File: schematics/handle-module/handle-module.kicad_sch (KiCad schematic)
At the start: 34 parts, among them J1 Conn_01x02_Socket, J11 USBASP, J2 XY-MK-5V@433MHz, J3 FS1000A@433Mhz, Q10 IRLML5203, Q14 IRLML0030, SW1 Close, SW2 Open, U1 AMS1117-5.0, U13 ATtiny1616-M, X2 CSX-750FCC, 16MHz

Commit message: Creating schematics and boards
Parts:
- removed C19 (x4): 22 uF, Capacitor_SMD:C_1210_3225Metric, symbol Device:C
- removed C22, C29: 100 nF, Capacitor_SMD:C_0603_1608Metric, symbol Device:C
- removed J11: USBASP, Connector_PinHeader_2.54mm:PinHeader_2x05_P2.54mm_Vertical, symbol Connector_Generic:Conn_02x05_Odd_Even
- removed J2: XY-MK-5V@433MHz, symbol Connector:Conn_01x04_Socket
- removed JP4: Jumper_2_Open, TestPoint:TestPoint_2Pads_Pitch2.54mm_Drill0.8mm, symbol Jumper:Jumper_2_Open
- removed Q14: IRLML0030, Package_TO_SOT_SMD:SOT-23, symbol Transistor_FET:IRLML0030
- removed R15, R29: 10K, Resistor_SMD:R_0805_2012Metric, symbol Device:R
- removed R15 (x2): 8K2, Resistor_SMD:R_0805_2012Metric, symbol Device:R
- removed U1: AMS1117-5.0, Package_TO_SOT_SMD:SOT-223-3_TabPin2, symbol Regulator_Linear:AMS1117-3.3
- removed U13: ATtiny1616-M, Package_DFN_QFN:VQFN-20-1EP_3x3mm_P0.4mm_EP1.7x1.7mm, symbol MCU_Microchip_ATtiny:ATtiny1616-M
- removed X2: CSX-750FCC, 16MHz, Oscillator:Oscillator_SMD_Abracon_ASE-4Pin_3.2x2.5mm, symbol Oscillator:SG-211
- added C14, C18, C21, C26 (x8): 100 nF, Capacitor_SMD:C_0603_1608Metric, symbol Device:C
- added C18, C26 (x2): 1 uF, Capacitor_SMD:C_0603_1608Metric, symbol Device:C
- added C26 (x2): 47 nF, Capacitor_SMD:C_0603_1608Metric, symbol Device:C
- added C26 (x4): 2.2 uF, Capacitor_SMD:C_0603_1608Metric, symbol Device:C
- added C26: 10 nF, Capacitor_SMD:C_0603_1608Metric, symbol Device:C
- added C26: 10 uF, Capacitor_SMD:C_0603_1608Metric, symbol Device:C
- added C26: 1 nF, Capacitor_SMD:C_0603_1608Metric, symbol Device:C
- added C27, C28: 15 pF, Capacitor_SMD:C_0603_1608Metric, symbol Device:C
- added C29 (x7): 22 uF, Capacitor_SMD:C_1210_3225Metric, symbol Device:C
- added C5, C6: 100 uF, Capacitor_THT:CP_Radial_D6.3mm_P2.50mm, symbol Device:C_Polarized
- added D10, D9: ES2J, Diode_SMD:D_SMB, symbol Device:D
- added D16: BAV21WS, Diode_SMD:D_SOD-323F, symbol Device:D
- added D2, D7, D8: 15MQ030NPBF, Diode_SMD:D_SMA, symbol Device:D
- added F1, F2: 3A, Library:FuseHolder1808, symbol Device:Fuse
- added H1, H2, H3, H4: MountingHole, MountingHole:MountingHole_2.2mm_M2, symbol Mechanical:MountingHole
- added J2: JST XH B3B, symbol Connector:Conn_01x03_Pin
- added J4: USBASP, Connector_PinHeader_2.54mm:PinHeader_2x05_P2.54mm_Vertical, symbol Connector_Generic:Conn_02x05_Odd_Even
- added JP1: AC Detect, Jumper:SolderJumper-2_P1.3mm_Open_TrianglePad1.0x1.5mm, symbol Jumper:SolderJumper_2_Open
- added L1, L2: ?, symbol Device:L
- added L3: AMPLF0630, 8,2uH, Inductor_SMD:L_Abracon_ASPI-0630LR, symbol Device:L
- added NT1: AGND/PGND, NetTie:NetTie-2_SMD_Pad2.0mm, symbol Device:NetTie_2
- added Q3 (x8): IRLML0030, Package_TO_SOT_SMD:SOT-23, symbol Transistor_FET:IRLML0030
- added R15 (x4): 100K, Resistor_SMD:R_0805_2012Metric, symbol Device:R
- added R15 (x4): 10, Resistor_SMD:R_0805_2012Metric, symbol Device:R
- added R15: 2R, Resistor_SMD:R_0805_2012Metric, symbol Device:R
- added R15 (x5), R28 (x3): 10K, Resistor_SMD:R_0805_2012Metric, symbol Device:R
- added R15: 45K, Resistor_SMD:R_0805_2012Metric, symbol Device:R
- added R15: 4R7, Resistor_SMD:R_0805_2012Metric, symbol Device:R
- added R15 (x2): 0.01 R, Resistor_SMD:R_1206_3216Metric, symbol Device:R
- added R15: 6R8, Resistor_SMD:R_0805_2012Metric, symbol Device:R
- added R15 (x3): 4K, Resistor_SMD:R_0805_2012Metric, symbol Device:R
- added R15: 7K, Resistor_SMD:R_0805_2012Metric, symbol Device:R
- added RV1: JVR-05N180M, Varistor:RV_Disc_D7mm_W4.5mm_P5mm, symbol Device:Varistor
- added TP1: VBAT, TestPoint:TestPoint_Pad_D1.0mm, symbol Connector:TestPoint
- added TP2: GND, TestPoint:TestPoint_Plated_Hole_D2.0mm, symbol Connector:TestPoint
- added TP3: +5V, TestPoint:TestPoint_Pad_D1.0mm, symbol Connector:TestPoint
- added TP4: VSYS, TestPoint:TestPoint_Pad_D1.0mm, symbol Connector:TestPoint
- added TP5: CHG SUPPLY, TestPoint:TestPoint_Pad_D1.0mm, symbol Connector:TestPoint
- added TP6: ILIM, TestPoint:TestPoint_Pad_D1.0mm, symbol Connector:TestPoint
- added U1: STX882@443MHz, Library:STX882_Vertical, symbol My_Library:STX882
- added U12: ATmega328-A, Package_QFP:TQFP-32_7x7mm_P0.8mm, symbol MCU_Microchip_ATmega:ATmega328-A
- added U2: SRX882@443MHz, Library:SRX882_Vertical, symbol My_Library:SRX882
- added U3: AMS1117-5.0, Package_TO_SOT_SMD:SOT-223-3_TabPin2, symbol Regulator_Linear:AMS1117-5.0
- added U4: MCP1703T-3302E, Package_TO_SOT_SMD:SOT-23, symbol Regulator_Linear:AMS1117-3.3
- added U6: BQ24780S, Package_DFN_QFN:QFN-28-1EP_4x4mm_P0.4mm_EP2.6x2.6mm_ThermalVias, symbol My_Library:BQ24780S
- added X1: HC-49U, 8MHz, Crystal:Crystal_HC49-U_Vertical, symbol Device:Crystal
- J1: value Conn_01x02_Socket -> 2*LiFePo4@18650@1800mAh, 6,4V; footprint (none) -> Connector_PinSocket_2.54mm:PinSocket_1x02_P2.54mm_Vertical
- J3: value FS1000A@433Mhz -> JST XH B3B; footprint (none) -> Connector_JST:JST_XH_B3B-XH-A_1x03_P2.50mm_Vertical
- SW1: renamed from SW2; value Open -> KLS7-TS3601-5.0-180; footprint (none) -> Library:SW_PUSH_P6.5_W3.5; Поле4 (none) -> Open
- SW2: renamed from SW1; value Close -> KLS7-TS3601-5.0-180; footprint (none) -> Library:SW_PUSH_P6.5_W3.5; Поле4 (none) -> Close
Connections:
- net POWER_UP_SW2 is gone; now on net OPEN_BUTTON: D16.2 (A), SW1.2
- net +5V: now also C14.1, C21.1, C26.1, C26.1, C29.1, J4.2 (Pin_2), R15.2, R15.2, R15.2, R15.2, R28.1, R28.1, R28.2, TP3.1, U1.3 (VCC), U12.18 (AVCC), U12.20 (AREF), U12.4 (VCC), U12.6 (VCC), U2.3 (VCC), U2.4 (CS), U3.2 (VO); no longer J3.2 (Pin_2)
- net CLOSE_BUTTON: now also D16.2 (A), SW2.1, Q3.1 (G)
- net FM_IN: now also U12.11 (PD7), U2.5 (DATA)
- net FM_OUT: now also U1.2 (DATA), U12.1 (PD3); no longer J3.1 (Pin_1)
- net LED_GREEN#: now also U12.13 (PB1)
- net LED_RED#: now also U12.14 (PB2)
- net OPEN_BUTTON: now also Q3.1 (G)
- net POWER_UP_IC: now also U12.9 (PD5)
- net GNDPWR: now reaches J1.1 (Pin_1)
- net GNDPWR: now also J3.2 (Pin_2), C26.2, C26.2, C26.2, C29.2, C29.2, C29.2, C5.2, NT1.1, Q3.2 (S), R15.2, RV1.2, TP2.1, U6.29 (PGND)
- removed net +9V: J1.2 (Pin_2), SW1.1, SW2.1
- net GND renamed GNDA
- net GNDA: now also C14.2, C18.1, C18.1, C21.2, C26.1, C26.2, C26.2, C26.2, C26.2, C26.2, C26.2, C26.2, C26.2, C27.2, C28.2, C29.2, C29.2, C29.2, C29.2, C6.2, J4.10 (Pin_10), J4.8 (Pin_8), NT1.2, Q3.2 (S), Q3.2 (S), Q3.2 (S), R15.1, R15.2, R15.2, R15.2, U1.4 (GND), U12.21 (GND), U12.3 (GND), U12.5 (GND), U2.2 (GND), U2.6 (GND), U3.1 (GND), U4.1 (GND), U6.22 (AGND); no longer J3.3 (Pin_3)
- net POWER_UP: no longer names the net of D16.1 (K), D16.1 (K), D16.1 (K)
- net POWER_UP: now also D16.1 (K), Q3.1 (G), R15.1
- net POWER_UP_SW1 renamed VBAT
- net VBAT: now also SW1.1, C26.1, C26.2, C29.1, D8.2 (A), F1.2, R15.1, R15.2, R15.2, TP1.1; no longer D16.2 (A)
- new net: C26.1, R15.1, U6.28 (VCC)
- new net: C26.2, C26.2, Q3.1 (G), R15.1, R15.2
- new net: C26.2, Q3.3 (D), R15.1, R15.2, U6.13 (CMPIN)
- new net: C26.1, D9.2 (A), J3.3 (Pin_3)
- new net: C26.2, D10.2 (A), J3.1 (Pin_1)
- new net: C26.2, R15.1
- new net: C28.1, U12.8 (XTAL2/PB7), X1.1
- new net: C27.1, U12.7 (XTAL1/PB6), X1.2
- new net: D7.1 (K), D8.1 (K), R15.2
- new net: R15.1, U6.5 (ACOK)
- new net: D10.1 (K), D9.1 (K), F2.1
- new net: C26.1, C26.1, Q3.3 (D), R15.1, U6.2 (ACP)
- new net: C29.1, D2.1 (K), U3.3 (VI)
- new net: JP1.1 (A), R15.1, R15.2
- new net: JP1.2 (B), U6.6 (ACDET)
- new net: J2.1 (Pin_1), L2.1
- new net: J2.2 (Pin_2), L1.1, L2.2
- new net: Q3.1 (G), R15.1
- new net: C26.1, R15.1
- new net: R15.1, U6.16 (TB_STAT#)
- new net: R15.2, U6.17 (BATSRC)
- new net: R15.2, U6.18 (BATDRV)
- new net: Q3.1 (G), U6.23 (LODRV)
- new net: C26.1, U6.24 (REGN)
- new net: Q3.1 (G), U6.26 (HIDRV)
- new net: R15.2, U6.3 (CMSRC)
- new net: R15.2, U6.4 (ACDRV)
- new net: J2.3 (Pin_3), L1.2
- new net +3V3: C18.2, R15.1, U4.2 (VO)
- new net CHARGER_BATDRV: Q3.1 (G), R15.1
- new net CHARGER_BATSRC: C26.1, C26.1, L3.2, Q3.2 (S), R15.1, R15.1, R15.2
- new net CHARGER_BOOST: R15.2, U6.25 (BTST)
- new net CHARGER_ILIM: R15.1, R15.2, TP6.1, U6.21 (ILIM)
- new net CHARGER_PHASE: C26.2, L3.1, Q3.2 (S), Q3.3 (D), U6.27 (PHASE)
- new net CHARGER_SRN: R15.2, U6.19 (SRN)
- new net CHARGER_SRP: R15.1, U6.20 (SRP)
- new net CHARGER_SUPPLY: C26.1, C26.1, C26.1, D16.2 (A), D7.2 (A), F2.2, Q3.3 (D), R15.1, RV1.1, TP5.1
- new net CHR_VSYS_NMOS: C26.1, Q3.2 (S), Q3.2 (S), R15.1
- new net CLOSE_BUTTON_5V#: Q3.3 (D), R15.1, U12.12 (PB0)
- new net MISO: J4.9 (Pin_9), U12.16 (PB4)
- new net MOSI: J4.1 (Pin_1), U12.15 (PB3)
- new net OPEN_BUTTON_5V#: Q3.3 (D), R15.1, U12.10 (PD6)
- new net RESET#: C26.1, J4.5 (Pin_5), R28.1, U12.29 (~{RESET}/PC6)
- new net RXD: J4.4 (Pin_4), U12.30 (PD0)
- new net SCK: J4.7 (Pin_7), U12.17 (PB5)
- new net SCL: R28.2, U12.28 (PC5), U6.12 (SCL)
- new net SDA: R28.2, U12.27 (PC4), U6.11 (SDA)
- new net TXD: J4.6 (Pin_6), U12.31 (PD1)
- new net VBAT_BEFORE_FUSE: C18.2, C26.1, C29.1, C5.1, C6.1, F1.1, J1.2 (Pin_2)
- new net VSYS: C26.1, C26.2, C29.1, C29.1, C29.1, D2.2 (A), Q3.3 (D), Q3.3 (D), R15.2, TP4.1, U4.3 (VI), U6.1 (ACN)
- no-connect marks 7 -> 16
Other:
- note added: "0.1A"
- note added: "0.5A"
- note added: "2A"
- note added: "AVG 1A MAX 2A"
- note added: "Program ATMega"
- note added: "REG0x3B[7] = 1"
- note added: "Test required"
- note removed: "ATTiny program port"
- note removed: "vdd cap"
- moved on the sheet: C18, D16, D8, J1, Q10, R15, R18, R54, SW1, SW2

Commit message: Second board
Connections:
- net GNDA: now also C26.2
- net GNDPWR: no longer C26.2
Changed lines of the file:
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@@
     )
   )
+  (symbol (lib_id "power:GNDA") (at 358.14 140.97 0) (unit 1)
+    (in_bom yes) (on_board yes) (dnp no)
+    (property "Reference" "#PWR053" (at 358.14 147.32 0)
+      (effects (font (size 1.27 1.27)) hide)
+    )
+    (property "Value" "GNDA" (at 358.14 146.05 0)
+      (effects (font (size 1.27 1.27)))
+    )
+    (property "Footprint" "" (at 358.14 140.97 0)
+      (effects (font (size 1.27 1.27)) hide)
+    )
+    (property "Datasheet" "" (at 358.14 140.97 0)
+      (effects (font (size 1.27 1.27)) hide)
+    )
+    (pin "1")
+    (instances
+      (project "handle-module"
+        (path "/5a1662b2-39be-45fc-af40-ee8b9104876f"
+          (reference "#PWR053") (unit 1)
+        )
+      )
+    )
+  )
   (symbol (lib_id "Device:C") (at 323.85 351.79 0) (unit 1)
     (in_bom yes) (on_board yes) (dnp no) (fields_autoplaced)
@@
         )
       )
-    )
-  )
-  (symbol (lib_id "power:GNDPWR") (at 358.14 140.97 0) (unit 1)
-    (in_bom yes) (on_board yes) (dnp no)
-    (property "Reference" "#PWR053" (at 358.14 146.05 0)
-      (effects (font (size 1.27 1.27)) hide)
-    )
-    (property "Value" "GNDPWR" (at 358.013 144.78 0)
-      (effects (font (size 1.27 1.27)))
-    )
-    (property "Footprint" "" (at 358.14 142.24 0)
-      (effects (font (size 1.27 1.27)) hide)
-    )
-    (property "Datasheet" "" (at 358.14 142.24 0)
-      (effects (font (size 1.27 1.27)) hide)
-    )
-    (pin "1")
-    (instances
-      (project "handle-module"
-        (path "/5a1662b2-39be-45fc-af40-ee8b9104876f"
-          (reference "#PWR053") (unit 1)
-        )
-      )

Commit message: Project prepared to order
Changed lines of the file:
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@@
     (stroke (width 0) (type default))
   )
+  (wire (pts (xy 153.67 21.59) (xy 153.67 26.67))
+    (stroke (width 0) (type default))
+  )
   (wire (pts (xy 215.9 124.46) (xy 233.68 124.46))
     (stroke (width 0) (type default))
@@
     (effects (font (size 1.27 1.27)) (justify right bottom))
   )
+  (label "VSYS" (at 153.67 26.67 270) (fields_autoplaced)
+    (effects (font (size 1.27 1.27)) (justify right bottom))
+  )
   (label "CHARGER_BATSRC" (at 421.64 154.94 180) (fields_autoplaced)
     (effects (font (size 1.27 1.27)) (justify right bottom))
@@
         )
       )
+    )
+  )
+  (symbol (lib_id "power:PWR_FLAG") (at 153.67 21.59 0) (unit 1)
+    (in_bom yes) (on_board yes) (dnp no) (fields_autoplaced)
+    (property "Reference" "#FLG07" (at 153.67 19.685 0)
+      (effects (font (size 1.27 1.27)) hide)
+    )
+    (property "Value" "PWR_FLAG" (at 153.67 16.51 0)
+      (effects (font (size 1.27 1.27)))
+    )
+    (property "Footprint" "" (at 153.67 21.59 0)
+      (effects (font (size 1.27 1.27)) hide)
+    )
+    (property "Datasheet" "~" (at 153.67 21.59 0)
+      (effects (font (size 1.27 1.27)) hide)
+    )
+    (pin "1")
+    (instances
+      (project "handle-module"
+        (path "/5a1662b2-39be-45fc-af40-ee8b9104876f"
+          (reference "#FLG07") (unit 1)
+        )
+      )

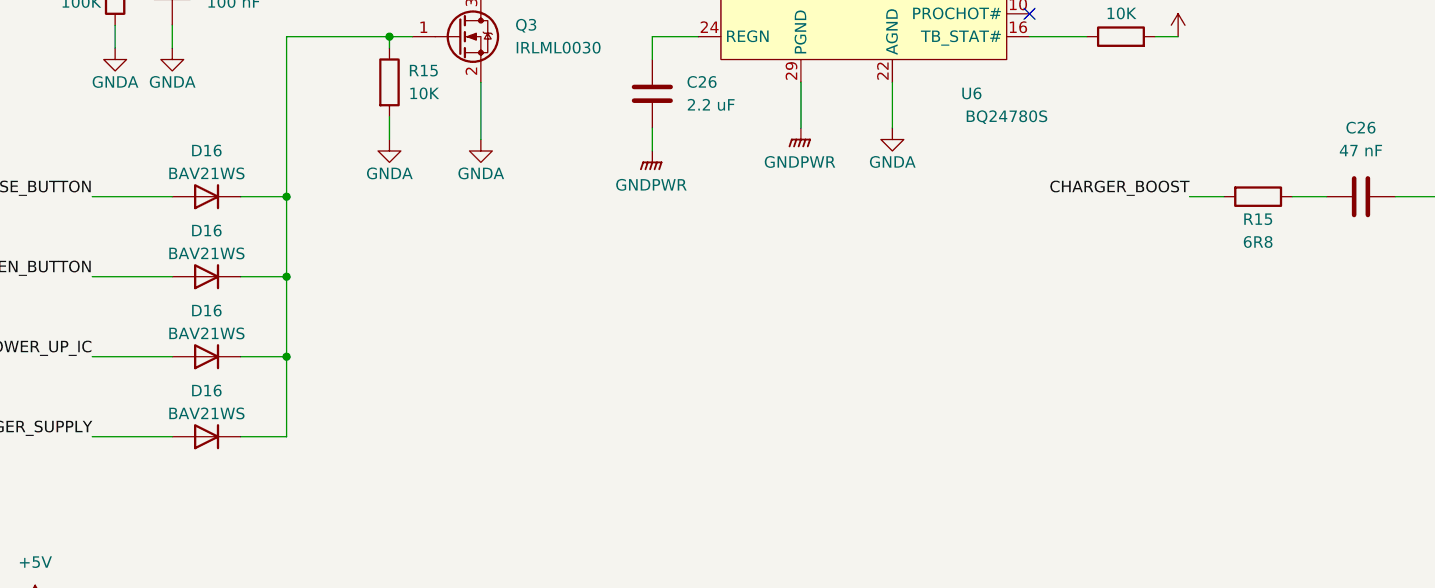
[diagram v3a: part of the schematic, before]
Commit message: first version of main-module firmware. not tested yet.
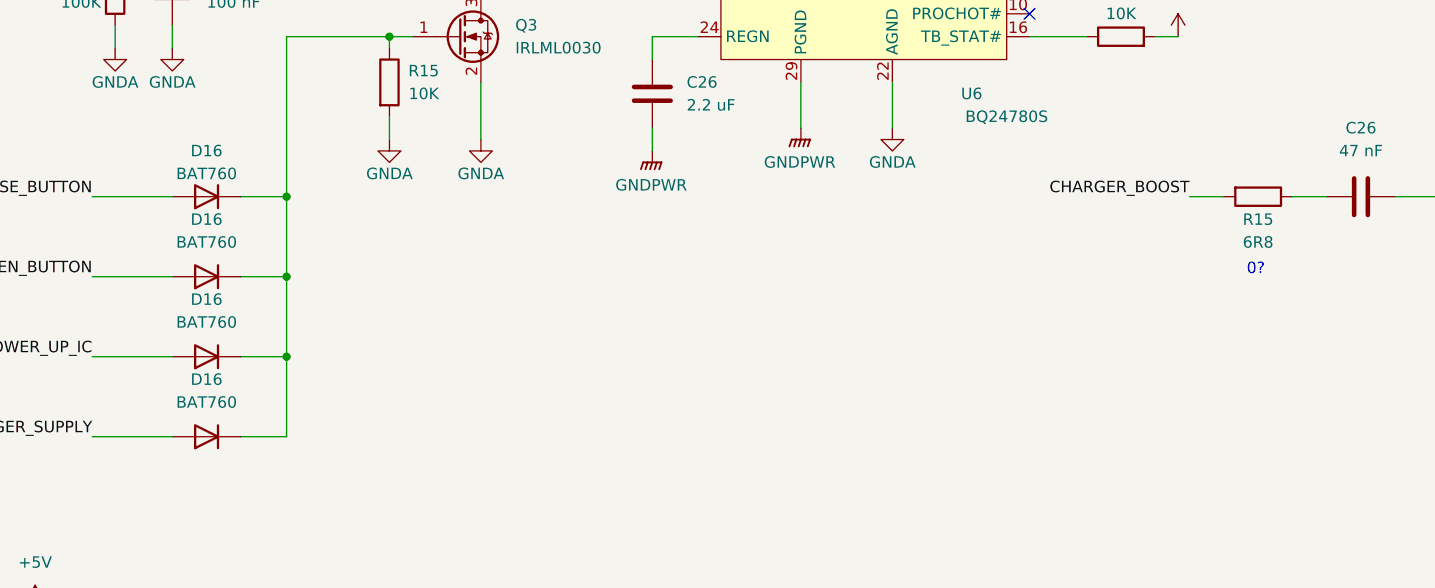
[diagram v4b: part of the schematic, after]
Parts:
- D16: value BAV21WS -> BAT760
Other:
- note added: "0?"
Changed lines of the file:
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@@
     (effects (font (size 1.27 1.27)) (justify left bottom))
   )
+  (text "0?" (at 361.95 247.65 0)
+    (effects (font (size 1.27 1.27)) (justify left bottom))
+  )
   (text "2A" (at 76.2 27.94 0)
     (effects (font (size 1.27 1.27)) (justify left bottom))
@@
   (symbol (lib_id "Device:D") (at 246.38 256.54 180) (unit 1)
     (in_bom yes) (on_board yes) (dnp no) (fields_autoplaced)
-    (property "Reference" "D16" (at 246.38 251.46 0)
+    (property "Reference" "D16" (at 246.38 250.19 0)
       (effects (font (size 1.27 1.27)))
     )
-    (property "Value" "BAV21WS" (at 246.38 254 0)
+    (property "Value" "BAT760" (at 246.38 252.73 0)
       (effects (font (size 1.27 1.27)))
     )
@@
   (symbol (lib_id "Device:D") (at 246.38 247.65 180) (unit 1)
     (in_bom yes) (on_board yes) (dnp no) (fields_autoplaced)
-    (property "Reference" "D16" (at 246.38 242.57 0)
+    (property "Reference" "D16" (at 246.38 241.3 0)
       (effects (font (size 1.27 1.27)))
     )
-    (property "Value" "BAV21WS" (at 246.38 245.11 0)
+    (property "Value" "BAT760" (at 246.38 243.84 0)
       (effects (font (size 1.27 1.27)))
     )
@@
       (effects (font (size 1.27 1.27)))
     )
-    (property "Value" "BAV21WS" (at 246.38 236.22 0)
+    (property "Value" "BAT760" (at 246.38 236.22 0)
       (effects (font (size 1.27 1.27)))
     )
@@
   (symbol (lib_id "Device:D") (at 246.38 265.43 180) (unit 1)
     (in_bom yes) (on_board yes) (dnp no) (fields_autoplaced)
-    (property "Reference" "D16" (at 246.38 260.35 0)
+    (property "Reference" "D16" (at 246.38 259.08 0)
       (effects (font (size 1.27 1.27)))
     )
-    (property "Value" "BAV21WS" (at 246.38 262.89 0)
+    (property "Value" "BAT760" (at 246.38 261.62 0)
       (effects (font (size 1.27 1.27)))
     )

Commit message: Working under firmwares
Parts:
- C18: value 10 nF -> 100 nF
- C18, C26: value 1 uF -> 2.2 uF
- C26: value 10 uF -> 4.7 uF
- R15: value 2R -> 5R
- R15: value 4R7 -> 10
- R15: value 4K -> 3K3
- R18: value 1K -> 620
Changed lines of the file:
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@@
       (effects (font (size 1.27 1.27)) (justify left))
     )
-    (property "Value" "1 uF" (at 361.95 135.89 0)
+    (property "Value" "2.2 uF" (at 361.95 135.89 0)
       (effects (font (size 1.27 1.27)) (justify left))
     )
@@
       (effects (font (size 1.27 1.27)))
     )
-    (property "Value" "2R" (at 194.31 167.64 0)
+    (property "Value" "5R" (at 194.31 167.64 0)
       (effects (font (size 1.27 1.27)))
     )
@@
       (effects (font (size 1.27 1.27)) (justify left))
     )
-    (property "Value" "10 uF" (at 461.01 43.18 0)
+    (property "Value" "4.7 uF" (at 461.01 43.18 0)
       (effects (font (size 1.27 1.27)) (justify left))
     )
@@
       (effects (font (size 1.27 1.27)) (justify right))
     )
-    (property "Value" "10 nF" (at 81.28 156.21 0)
+    (property "Value" "100 nF" (at 81.28 156.21 0)
       (effects (font (size 1.27 1.27)) (justify right))
     )
@@
       (effects (font (size 1.27 1.27)))
     )
-    (property "Value" "4R7" (at 252.73 142.24 0)
+    (property "Value" "10" (at 252.73 142.24 0)
       (effects (font (size 1.27 1.27)))
     )
@@
       (effects (font (size 1.27 1.27)) (justify right))
     )
-    (property "Value" "1 uF" (at 270.51 68.58 0)
+    (property "Value" "2.2 uF" (at 270.51 68.58 0)
       (effects (font (size 1.27 1.27)) (justify right))
     )
@@
       (effects (font (size 1.27 1.27)))
     )
-    (property "Value" "4K" (at 251.46 172.72 0)
+    (property "Value" "3K3" (at 251.46 172.72 0)
       (effects (font (size 1.27 1.27)))
     )
@@
       (effects (font (size 1.27 1.27)) (justify right))
     )
-    (property "Value" "10 nF" (at 80.01 212.09 0)
+    (property "Value" "100 nF" (at 80.01 212.09 0)
       (effects (font (size 1.27 1.27)) (justify right))
     )
@@
   (symbol (lib_id "Device:R") (at 102.87 351.79 90) (unit 1)
     (in_bom yes) (on_board yes) (dnp no) (fields_autoplaced)
-    (property "Reference" "R18" (at 102.87 346.71 90)
+    (property "Reference" "R18" (at 102.87 345.44 90)
       (effects (font (size 1.27 1.27)))
     )
-    (property "Value" "1K" (at 102.87 349.25 90)
+    (property "Value" "620" (at 102.87 347.98 90)
       (effects (font (size 1.27 1.27)))
     )
@@
       (effects (font (size 1.27 1.27)) (justify left))
     )
-    (property "Value" "1 uF" (at 152.4 49.53 0)
+    (property "Value" "2.2 uF" (at 152.4 49.53 0)
       (effects (font (size 1.27 1.27)) (justify left))
     )
@@
       (effects (font (size 1.27 1.27)))
     )
-    (property "Value" "4K" (at 350.52 167.64 90)
+    (property "Value" "3K3" (at 350.52 167.64 90)
       (effects (font (size 1.27 1.27)))
     )
@@
       (effects (font (size 1.27 1.27)))
     )
-    (property "Value" "4K" (at 270.51 172.72 0)
+    (property "Value" "3K3" (at 270.51 172.72 0)
       (effects (font (size 1.27 1.27)))
     )

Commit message: 1. first 3D models, 2. charger works
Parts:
- R15: value 10 -> 5
- R15: value 3K3 -> 3K9
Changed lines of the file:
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@@
       (effects (font (size 1.27 1.27)))
     )
-    (property "Value" "10" (at 252.73 142.24 0)
+    (property "Value" "5" (at 252.73 142.24 0)
       (effects (font (size 1.27 1.27)))
     )
@@
       (effects (font (size 1.27 1.27)))
     )
-    (property "Value" "3K3" (at 251.46 172.72 0)
+    (property "Value" "3K9" (at 251.46 172.72 0)
       (effects (font (size 1.27 1.27)))
     )
@@
       (effects (font (size 1.27 1.27)))
     )
-    (property "Value" "3K3" (at 270.51 172.72 0)
+    (property "Value" "3K9" (at 270.51 172.72 0)
       (effects (font (size 1.27 1.27)))
     )

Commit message: change nominal
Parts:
- R15: value 7K -> 62K
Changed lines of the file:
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@@
       (effects (font (size 1.27 1.27)))
     )
-    (property "Value" "7K" (at 500.38 142.24 0)
+    (property "Value" "62K" (at 500.38 142.24 0)
       (effects (font (size 1.27 1.27)))
     )

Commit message: 1. board: added protection against high noise in case of endstop is broken. 2. board: added step-up 7.5V -> 15V for charger. 3. firmware - added support for noise protection and some changes in stepper logic
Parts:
- removed C18: 2.2 uF, Capacitor_SMD:C_0603_1608Metric, symbol Device:C
- removed C26: 10 nF, Capacitor_SMD:C_0603_1608Metric, symbol Device:C
- removed C26: 100 nF, Capacitor_SMD:C_0603_1608Metric, symbol Device:C
- removed C29: 22 uF, Capacitor_SMD:C_1210_3225Metric, symbol Device:C
- removed D10: ES2J, Diode_SMD:D_SMB, symbol Device:D
- removed D16 (x4): BAT760, Diode_SMD:D_SOD-323F, symbol Device:D
- removed J2: JST XH B3B, symbol Connector:Conn_01x03_Pin
- removed J3: JST XH B3B, Connector_JST:JST_XH_B3B-XH-A_1x03_P2.50mm_Vertical, symbol Connector:Conn_01x03_Socket
- removed JP1: AC Detect, Jumper:SolderJumper-2_P1.3mm_Open_TrianglePad1.0x1.5mm, symbol Jumper:SolderJumper_2_Open
- removed L1, L2: ?, symbol Device:L
- removed Q3: IRLML0030, Package_TO_SOT_SMD:SOT-23, symbol Transistor_FET:IRLML0030
- removed R15 (x3): 100K, Resistor_SMD:R_0805_2012Metric, symbol Device:R
- removed R15 (x2): 10K, Resistor_SMD:R_0805_2012Metric, symbol Device:R
- removed R15: 6R8, Resistor_SMD:R_0805_2012Metric, symbol Device:R
- removed R15: 62K, Resistor_SMD:R_0805_2012Metric, symbol Device:R
- removed U4: MCP1703T-3302E, Package_TO_SOT_SMD:SOT-23, symbol Regulator_Linear:AMS1117-3.3
- added D3, D4, D5: BAT760, Diode_SMD:D_SOD-323F, symbol Device:D
- added D7: SMAJ26A, Diode_SMD:D_SMA, symbol Diode:SMAJ26A
- added H5: MountingHole, MountingHole:MountingHole_2.2mm_M2, symbol Mechanical:MountingHole
- added J2: Charger, Connector_JST:JST_XH_B2B-XH-A_1x02_P2.50mm_Vertical, symbol Connector:Conn_01x02_Socket
- added Q5: IRLML0030, Package_TO_SOT_SMD:SOT-23, symbol Transistor_FET:IRLML0030
- added Q6: IRLML5203, Package_TO_SOT_SMD:SOT-23, symbol Transistor_FET:IRLML5203
- added R10, R9: 10K, Resistor_SMD:R_0805_2012Metric, symbol Device:R
- added R23: 500, Resistor_SMD:R_0805_2012Metric, symbol Device:R
- added TP3: ACDRV, TestPoint:TestPoint_Pad_D1.0mm, symbol Connector:TestPoint
- added TP4: ACDET, TestPoint:TestPoint_Pad_D1.0mm, symbol Connector:TestPoint
- D2: value 15MQ030NPBF -> BAT760; footprint Diode_SMD:D_SMA -> Diode_SMD:D_SOD-323F
- TP2: footprint TestPoint:TestPoint_Plated_Hole_D2.0mm -> Library:TestPoint_Plated_Hole_D1.0mm
- TP6: value ILIM -> ACOK
- renumbered D7 to D6, L3 to L1, TP3 to TP5, TP5 to TP7, TP4 to TP8, U3 to U4, U6 to U5
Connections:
- net CHARGER_BOOST is gone; now on an unnamed net: U5.25 (BTST)
- net CHARGER_SUPPLY: now also D5.2 (A)
- net CLOSE_BUTTON: now also D2.2 (A)
- net GNDA: now also U5.21 (ILIM), Q5.2 (S), R10.2
- net GNDPWR: now also D7.2 (A2), J2.1 (Pin_1), R23.2
- net OPEN_BUTTON: now also D3.2 (A)
- net VSYS: now also Q6.2 (S), R9.1; no longer D2.2 (A)
- net at C26.2, C26.2, Q3.1 (G)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: now also TP3.1
- net at D9.2 (A): now also D7.1 (A1), J2.2 (Pin_2), R23.1
- net at R15.1, U5.5 (ACOK): now also TP6.1
- net at C29.1, U4.3 (VI): now also Q6.3 (D); no longer D2.1 (K)
- net at R15.1, R15.2: now also U5.6 (ACDET), TP4.1
- removed net CHARGER_ILIM: TP6.1, U5.21 (ILIM)
- net CHARGER_PHASE: no longer names the net of C26.2, L1.1, Q3.2 (S), Q3.3 (D), U5.27 (PHASE)
- net POWER_UP_IC renamed IC_POWER_UP
- net IC_POWER_UP: now also D4.2 (A)
- new net: D2.1 (K), D3.1 (K), D4.1 (K), D5.1 (K), Q5.1 (G), R10.1
- new net: Q5.3 (D), Q6.1 (G), R9.2
- no-connect marks 16 -> 18
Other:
- note removed: "0.1A"
- note removed: "0?"
- note removed: "REG0x3B[7] = 1"
- note removed: "Test required"
- moved on the sheet: C18, C26, C29, D6, D8, D9, L1, Q3, R15, SW1, SW2, TP5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
